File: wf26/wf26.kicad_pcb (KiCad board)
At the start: 2 copper layers, 40.5 x 37.2 mm, 7 parts, among them J1 WF26 -> TV20 S bus, K1 HJR-4102-N-12V

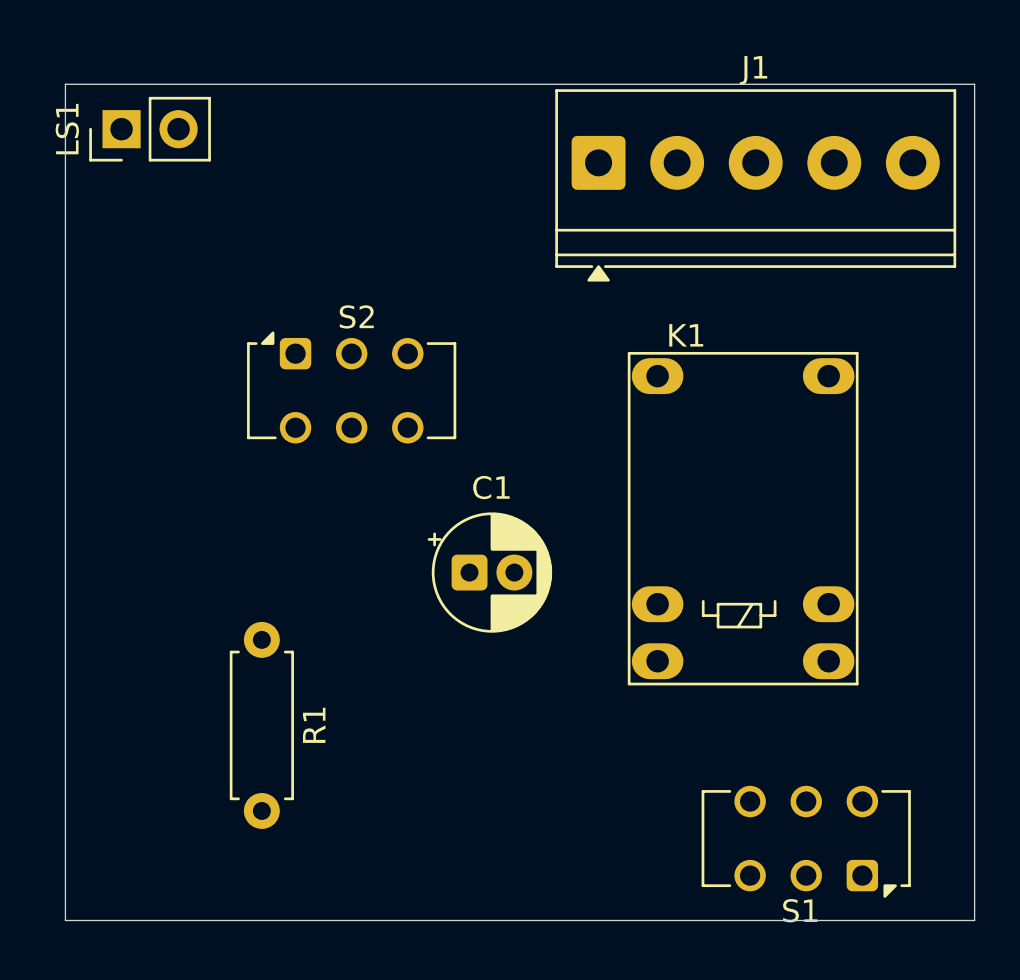
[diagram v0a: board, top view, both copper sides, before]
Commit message: WF26: correct relay symbol pinout (pin 6 = NO) and reconcile docs/notes
Confirmed via datasheet + in-circuit continuity that the WF26 internal
relay's P2 sits on the normally-open contact = HJR-4102 pin 6 (the symbol
had NO/NC swapped):
- sym/wf26.kicad_sym: pin 6 = NO, pin 7 = NC; pins reordered to a
  consistent top-view layout (1/12 and 5/8 swaps are no-ops: COM tied,
  coil symmetric)
- schematic notes: talk/listen via WF26_K1 NO; refdes K1 -> WF26_K1;
  line 5/P5 reaches the bus via the external Etagenruf (ET) button
- DESIGN.md: relay pinout, refdes (WF26_K1 / K1_COM / OT_BRIDGE), speech
  on bus pair 2/3 coupled into LS1 via C1, Mithoersperre, talk=P4<->P3 /
  listen=P4<->P2; closed the NO/NC open item

Schematic relay net rewiring (P2 -> pin 6) + Update-from-Library still to
be applied in KiCad.
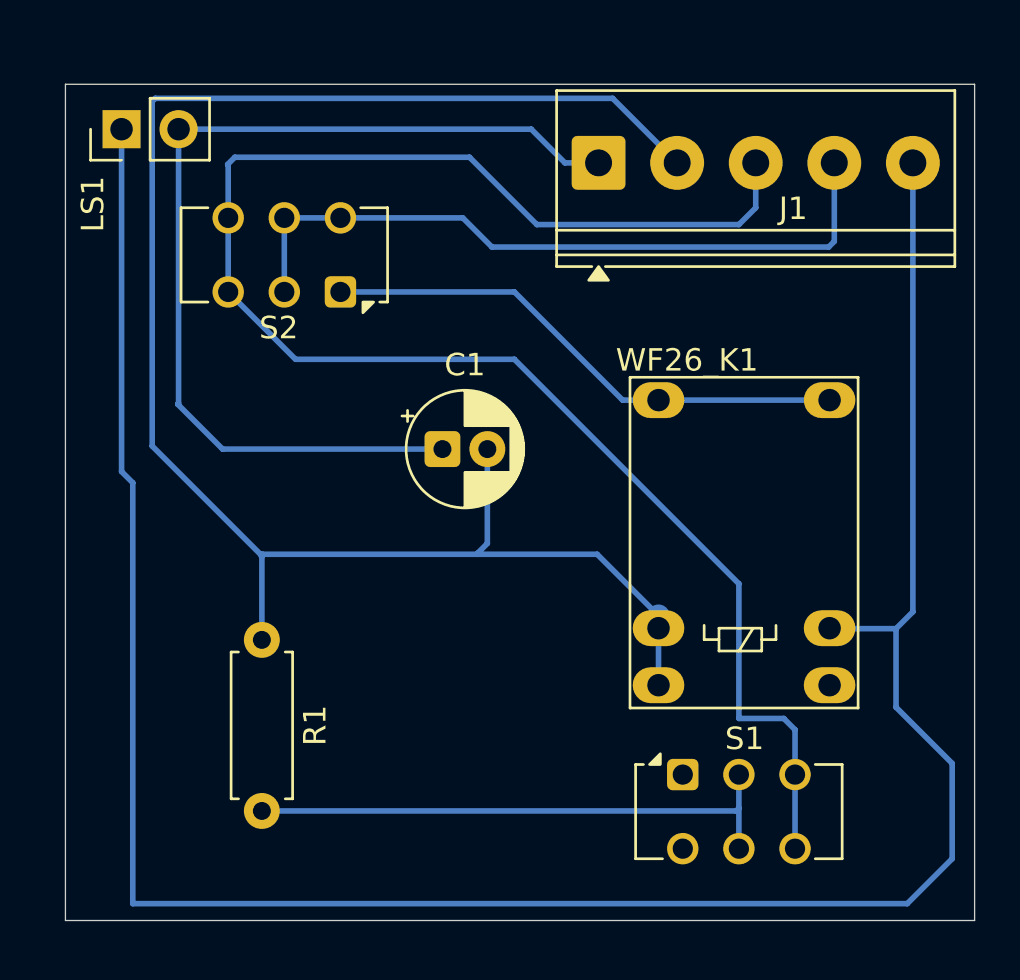
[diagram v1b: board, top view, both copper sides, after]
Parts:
- removed K1: HJR-4102-N-12V, Relay_THT:Relay_SPDT_HJR-4102
- added WF26_K1: HJR-4102-N-12V, Relay_THT:Relay_SPDT_HJR-4102, F.Cu at (48.4, 42.8)
- moved S1 9.18 mm to (49.5, 59.5), turned to 0 degrees
- moved C1 5.63 mm to (38.8, 45.0)
- moved S2 3.40 mm to (34.2, 38.0), turned to 180 degrees
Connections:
- R1 pad 1: unconnected-(R1-Pad1) -> /P2
- R1 pad 2: unconnected-(R1-Pad2) -> /OT_BRIDGE
- S1 pad 2: /S1_COM -> /OT_BRIDGE
- S1 pad 3: Net-(S1A-C) -> /P3
- S1 pad 4: Net-(S1A-C) -> /P3
- S1 pad 5: /S1_COM -> /OT_BRIDGE
- S2 pad 1: /P4 -> /K1_COM
- S2 pad 6: /K1_COM -> /P4
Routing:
- net /P5: track 0.00 -> 107.6 mm
- net /P2: track 0.00 -> 77.4 mm
- net /P3: track 0.00 -> 75.3 mm
- net /P1: track 0.00 -> 44.2 mm
- net /P4: track 0.00 -> 31.9 mm
- net /OT_BRIDGE: track 0.00 -> 24.6 mm
- net /K1_COM: track 0.00 -> 23.8 mm

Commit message: Correct WF26 internal model; rework DESIGN.md; add TODO + schematic readout
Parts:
- moved S2 26.5 mm to (49.5, 59.7), turned to 0 degrees
- moved S1 26.3 mm to (34.3, 38.0), turned to 180 degrees
- moved J1 14.0 mm to (59.8, 32.2), turned to 180 degrees
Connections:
- C1 pad 1: /P1 -> /P5
- C1 pad 2: /P2 -> /P4
- LS1 pad 1: /P5 -> /P1
- LS1 pad 2: /P1 -> /P5
- R1 pad 1: /P2 -> /P4
- R1 pad 2: /OT_BRIDGE -> /R1_BRIDGE
- S1 pad 1: unconnected-(S1-A-Pad1) -> /K1_COM
- S1 pad 2: /OT_BRIDGE -> /P2
- S1 pad 5: /OT_BRIDGE -> /P2
- S1 pad 6: unconnected-(S1-C-Pad6) -> /P2
- S2 pad 1: /K1_COM -> unconnected-(S2-A-Pad1)
- S2 pad 2: /P4 -> /R1_BRIDGE
- S2 pad 5: /P4 -> /R1_BRIDGE
- S2 pad 6: /P4 -> unconnected-(S2-C-Pad6)
- WF26_K1 pad 5: /P2 -> /P4
- WF26_K1 pad 6: /P2 -> /P4
- WF26_K1 pad 8: /P5 -> /P1
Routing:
- net /P5: track 107.6 -> 44.2 mm
- net /P1: track 44.2 -> 107.6 mm
- net /P4: track 31.9 -> 77.4 mm
- net /P2: track 77.4 -> 31.9 mm
- net /R1_BRIDGE: track 0.00 -> 24.6 mm
- net /OT_BRIDGE: track 24.6 -> 0.00 mm
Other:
- board size 40.5 x 37.2 mm -> 64 x 59 mm

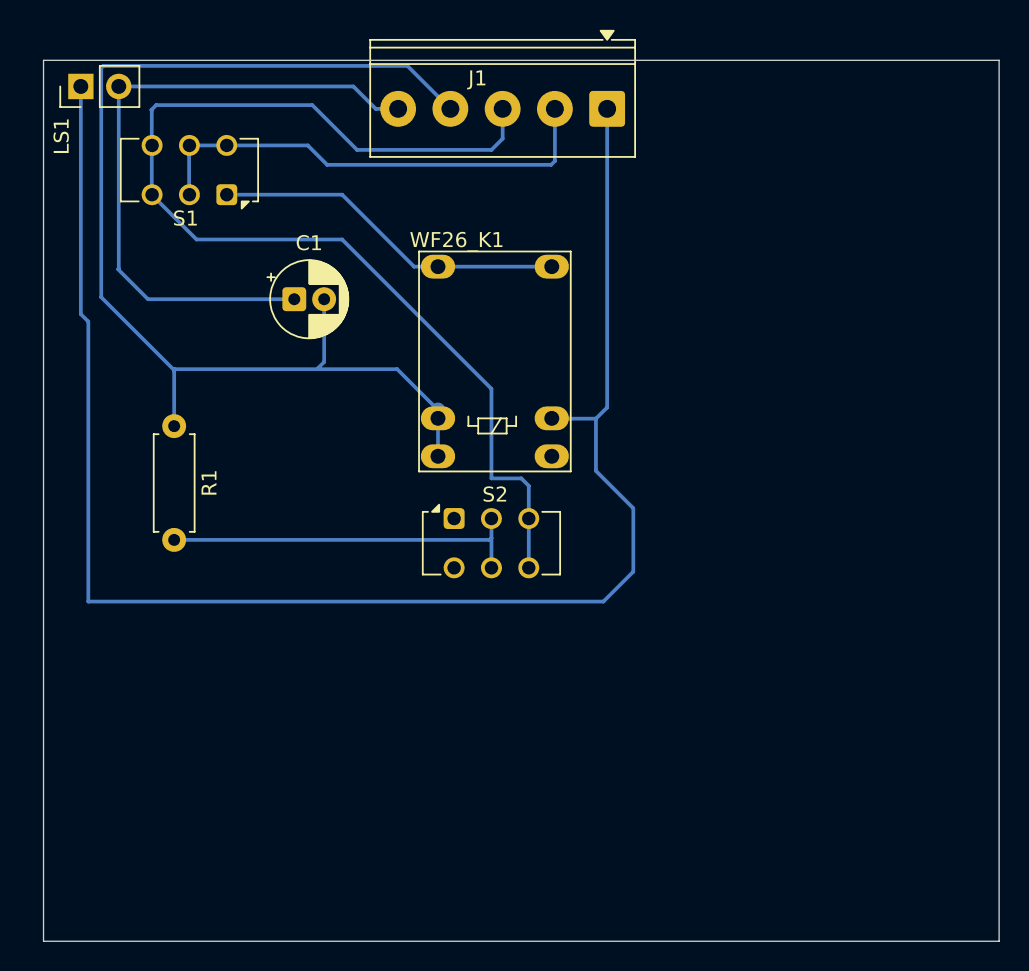
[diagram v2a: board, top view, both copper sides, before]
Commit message: V4: remove opto polarity switches (SW4/SW5), hardwire polarity
- Bus is taken to drive active lines positive w.r.t. P1, so each bell-sense opto
  LED is hardwired anode -> bus line (IN_P4 for OC1, P5 for OC2), cathode -> R_lim
  -> P1. SW4/SW5 (CAS-220 DPDT) deleted from schematic + PCB; clamps (D8/D9),
  limiters (R1/R2) and pull-ups (R22/R23) retained. Confirm per-channel polarity
  on the bench by ringing each bell.
- Verify: ERC 0 errors (pin_to_pin warnings 51->39); DRC clean (1 benign
  isolated-copper thieving warning); 0 unrouted, 0 unconnected.
- Docs: DESIGN.md (fixed-polarity decision, dropped switch refs), ORDERING.md
  (dropped SW3-5; also refreshed the stale D7 / OK1-3 -> OC1-2 / session refs),
  TODO.md. doorbell.pdf re-exported.

WF26 handset board: reposition S1 and the relay (WF26_K1).
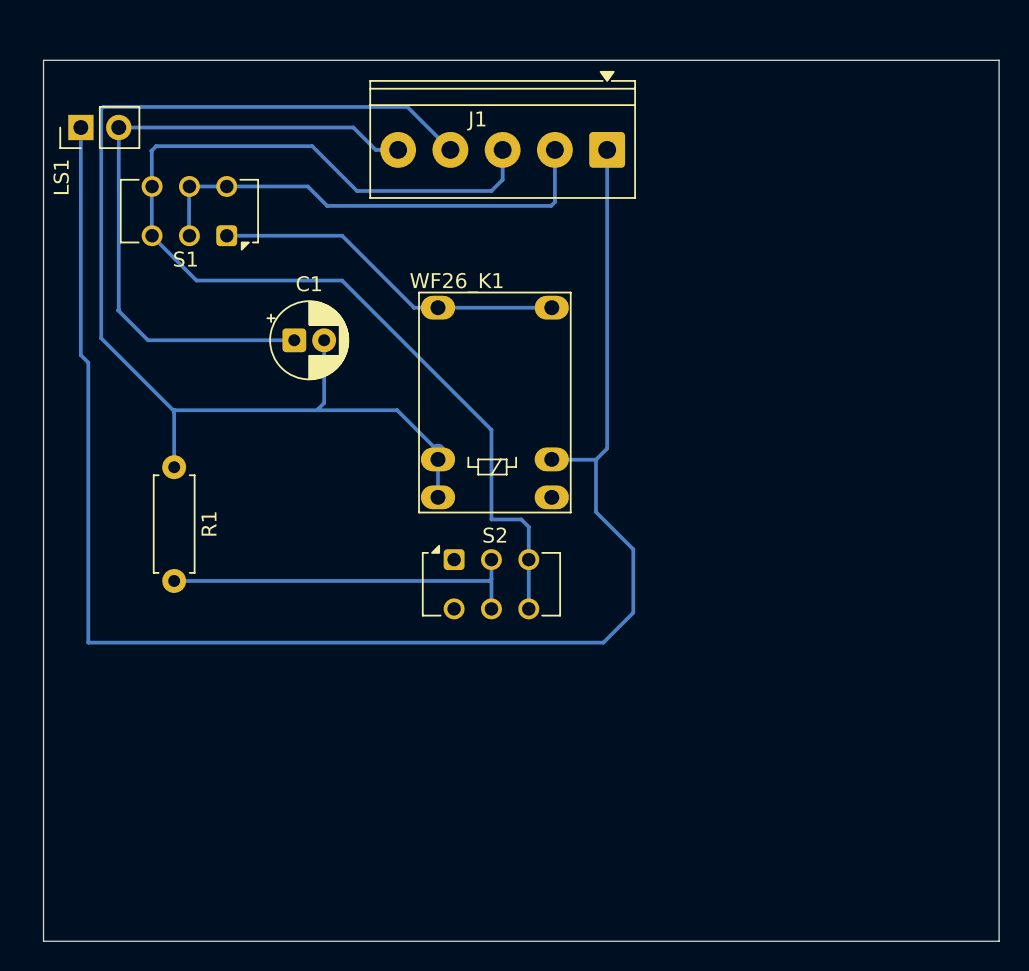
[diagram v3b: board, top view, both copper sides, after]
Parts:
- moved C1 2.75 mm to (38.8, 47.8)
- moved J1 2.75 mm to (59.8, 35.0)
- moved LS1 2.75 mm to (24.5, 33.5)
- moved R1 2.75 mm to (30.8, 56.2)
- moved S1 2.75 mm to (34.3, 40.8)
- moved S2 2.75 mm to (49.5, 62.4)
- moved WF26_K1 2.75 mm to (48.4, 45.6)

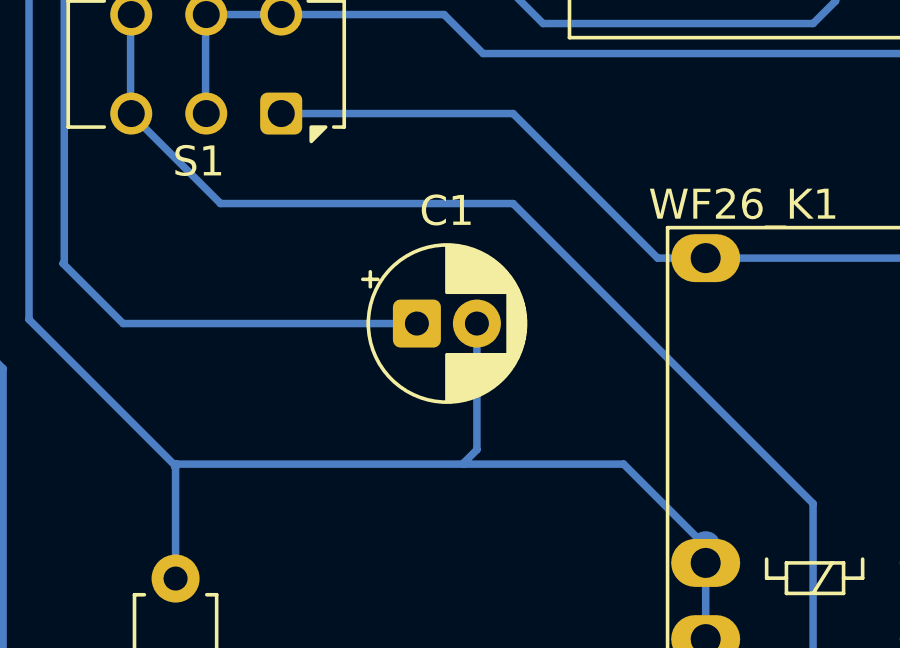
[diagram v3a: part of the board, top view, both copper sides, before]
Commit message: WF26 core + enclosure fit: relay→SMD, cap polarity, switches, 59mm trim
- WF26_K1: THT HJR-4102 → SMD Omron G6K-2F-Y DC12 (Relay:G6K-2, LCSC
  C397194); rewired as SPDT — coil P1↔WF26_P4, COM(3)→NO(4) routes the
  listen path, spare pole no-connected
- WF26_C1: polarity flipped (+ → WF26_P4, the Türruf +12 V side)
- WF26_S1/S2: ALPS SPPJ223200 momentary DPDT symbol; pinout relabeled
  COM/NC/NO + mounting posts
- PCB: board trimmed to 64 × 59 mm for the WF26 enclosure (Edge.Cuts +
  zone outlines); components re-floorplanned/rotated; S1/S2 plunger
  reference crosshairs added on Dwgs.User
- Docs: C1 polarity corrected in DESIGN.md (+ → P4) and TODO; add
  docs/CBM5D33 (Sumida ESMIT-4180/C datasheet)
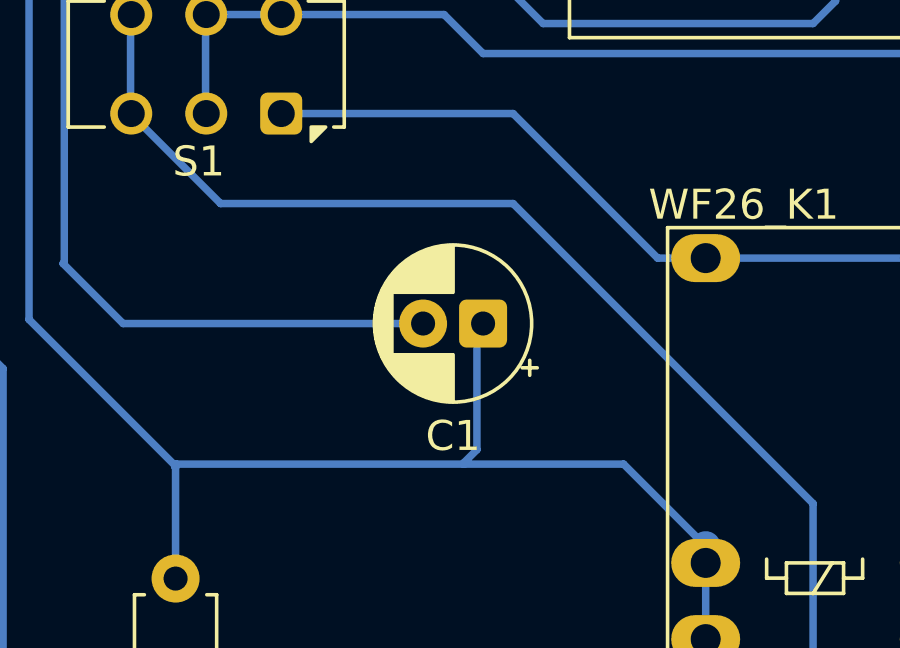
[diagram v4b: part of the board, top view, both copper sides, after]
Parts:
- moved C1 2.21 mm to (41.0, 47.8), turned to 180 degrees
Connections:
- C1 pad 1: /P5 -> /P4
- C1 pad 2: /P4 -> /P5
